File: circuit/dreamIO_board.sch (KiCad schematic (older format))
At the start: 49 parts

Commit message: finished circuit schematic. Needs review
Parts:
- added C? (x12): .1uF, symbol C
- added P?: CONN_01X03, symbol CONN_01X03
- added R? (x12): 150, symbol R
- added U? (x11): WS2812, symbol WS2812
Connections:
- net labels added: DOUT
- wire segments 154 -> 294
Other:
- note added: "MPU Connections"
- note added: "NeoPixel Output"
- moved on the sheet: C?, R?, U?

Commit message: added notes and updated circuit design
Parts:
- removed C? (x11): .1uF, symbol C
- removed R? (x11): 150, symbol R
- removed U? (x11): WS2812, symbol WS2812
- added C10, C11, C12, C15, C16, C17, C18, C19, C20, C21, C22: .1uF, symbol C
- added R13, R14, R15, R17, R18, R19, R20, R21, R22, R23, R24: 150, symbol R
- added U10, U11, U12, U13, U14, U15, U16, U6, U7, U8, U9: WS2812, symbol WS2812
- gave numbers to parts that had none: 52
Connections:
- wire segments 294 -> 258
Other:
- moved on the sheet: C9, R12

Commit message: added custom footprint for tsp61200 regulator
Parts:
- removed R13, R14, R15, R17, R18, R19, R20, R21, R22, R23, R24: 150, symbol R
- removed SW1: SPST, symbol SPST
- removed U10, U11, U12, U13, U14, U15, U16, U5, U6, U7, U8, U9: WS2812, symbol WS2812
- added LED1, LED10, LED11, LED12, LED2, LED3, LED4, LED5, LED6, LED7, LED8, LED9: WS2812B, kicad-libraries:WS2812B_LED, symbol WS2812B
- added SW1: SPDT, Buttons_Switches_ThroughHole:SW_Micro_SPST, symbol SPDT
- C1, C10, C11, C12, C13, C14, C15, C16, C17, C18, C19, C2, C20, C21, C22, C23, C24, C25, C26, C3, C4, C5, C6, C7, C8, C9, R1, R10, R11, R16, R2, R25, R26, R27, R3, R4, R5, R6, R7, R8, R9: footprint (none) -> kicad-libraries:0603
- D1: footprint (none) -> Capacitors_Tantalum_SMD:TantalC_SizeA_EIA-3216_HandSoldering
- IC1: footprint (none) -> Housings_DFN_QFN:DFN-10-1EP_3x3mm_Pitch0.5mm
- L1: footprint (none) -> kicad-libraries:1206E
- P1: value CONN_01X02 -> BATT; footprint (none) -> Pin_Headers:Pin_Header_Straight_1x02
- P2, P3, P5: footprint (none) -> Pin_Headers:Pin_Header_Straight_1x06
- P4, P6: footprint (none) -> Pin_Headers:Pin_Header_Straight_1x02
- P7: footprint (none) -> Pin_Headers:Pin_Header_Straight_1x03
- P8: footprint (none) -> Pin_Headers:Pin_Header_Straight_1x04
- P9: value CONN_01X03 -> PixelOut; footprint (none) -> Pin_Headers:Pin_Header_Straight_1x03
- R12: value 150 -> 220; footprint (none) -> kicad-libraries:0603
- SW2: value SW_PUSH -> RESET; footprint (none) -> shardy:SW_PUSH_SMALL
- SW3: value SW_PUSH -> PRGM; footprint (none) -> shardy:SW_PUSH_SMALL
- U1: footprint (none) -> kicad-libraries:SOT23-5
- U17: footprint (none) -> kicad-libraries:QFN-24-4x4-EP
- U2: footprint (none) -> open-project:MICRO-B_USB
- U3: footprint (none) -> kicad-libraries:SOT-223
- U4: footprint (none) -> ESP8266:ESP-12E
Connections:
- wire segments 258 -> 257
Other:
- moved on the sheet: C9, R12

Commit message: fixed IC1 footprint
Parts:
- IC1: footprint Housings_DFN_QFN:DFN-10-1EP_3x3mm_Pitch0.5mm -> tps61200_qfn_custom:tps61200_QFN-10_PAD
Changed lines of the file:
@@
 F 0 "IC1" H 4900 4400 50  0000 C CNN
 F 1 "TPS61200" H 5550 4400 50  0000 C CNN
-F 2 "Housings_DFN_QFN:DFN-10-1EP_3x3mm_Pitch0.5mm" H 5300 3800 60  0001 C CNN
+F 2 "tps61200_qfn_custom:tps61200_QFN-10_PAD" H 5300 3800 60  0001 C CNN
 F 3 "" H 5300 3800 60  0000 C CNN
 	1    5300 3800

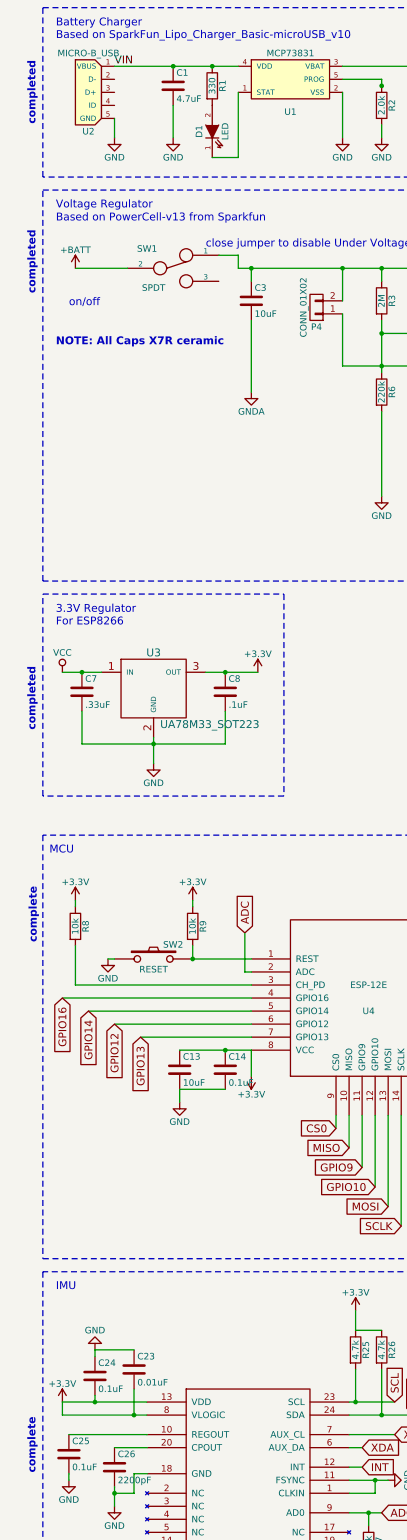
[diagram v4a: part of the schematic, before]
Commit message: grouped PCB components together for board:
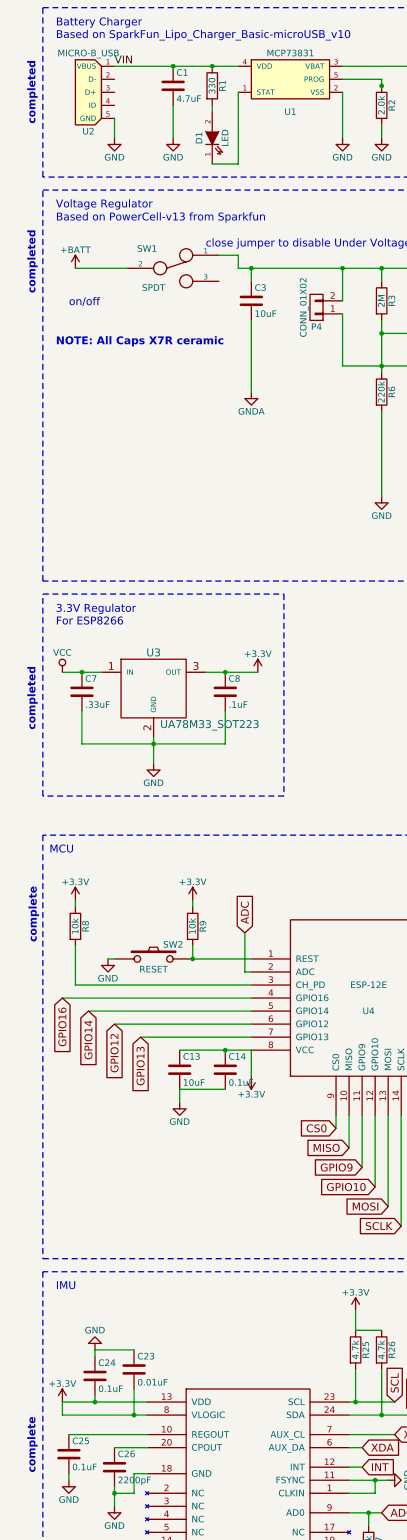
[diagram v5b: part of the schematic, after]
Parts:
- D1: footprint Capacitors_Tantalum_SMD:TantalC_SizeA_EIA-3216_HandSoldering -> kicad-libraries:0603
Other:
- moved on the sheet: D1
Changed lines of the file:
@@
 L LED D1
 U 1 1 56B0400A
-P 2500 1850
-F 0 "D1" H 2500 1950 50  0000 C CNN
-F 1 "LED" H 2500 1750 50  0000 C CNN
-F 2 "Capacitors_Tantalum_SMD:TantalC_SizeA_EIA-3216_HandSoldering" H 2500 1850 60  0001 C CNN
-F 3 "" H 2500 1850 60  0000 C CNN
-	1    2500 1850
+P 2500 1900
+F 0 "D1" H 2500 2000 50  0000 C CNN
+F 1 "LED" H 2500 1800 50  0000 C CNN
+F 2 "kicad-libraries:0603" H 2500 1900 60  0001 C CNN
+F 3 "" H 2500 1900 60  0000 C CNN
+	1    2500 1900
 	0    -1   -1   0
 $EndComp
@@
 	2000 12150 1900 12150
 Wire Wire Line
-	2000 11950 1750 11950
-Wire Wire Line
 	1750 12250 1750 12400
 Wire Wire Line
@@
 	2200 1650 2200 1900
 Wire Wire Line
-	2500 2050 2700 2050
-Wire Wire Line
-	2700 2050 2700 1550
+	2700 1550 2700 2100
 Wire Wire Line
 	1750 1350 2700 1350
@@
 Wire Wire Line
 	15200 11550 15700 11550
+Wire Wire Line
+	1750 11950 2000 11950
+Wire Wire Line
+	2500 1650 2500 1700
+Wire Wire Line
+	2700 2100 2500 2100
 $EndSCHEMATC

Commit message: finished layout
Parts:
- removed P2, P3: CONN_01X06, Pin_Headers:Pin_Header_Straight_1x06, symbol CONN_01X06
- removed P8: CONN_01X04, Pin_Headers:Pin_Header_Straight_1x04, symbol CONN_01X04
- added P2, P3: CONN_01X08, _connectors:_Pin2mm_8, symbol CONN_01X08
- P4: footprint Pin_Headers:Pin_Header_Straight_1x02 -> _connectors:_Solder_Pad2.54_2
- P5: footprint Pin_Headers:Pin_Header_Straight_1x06 -> _connectors:_Pin2mm_6
- P6: value CONN_01X02 -> gnd_con; footprint Pin_Headers:Pin_Header_Straight_1x02 -> _connectors:_Solder_Pad2.54_2
- P7: footprint Pin_Headers:Pin_Header_Straight_1x03 -> _connectors:_Solder_Pad2.54_3
- SW2, SW3: footprint shardy:SW_PUSH_SMALL -> kicad-libraries:SW_06_SMD
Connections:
- net +3V3: now also P2.8 (P8); no longer P5.6 (P6)
- net ADC: now also P2.2 (P2)
- net CS0: now also P5.1 (P1)
- net GND: now also P3.8 (P8); no longer P5.5 (P5)
- net GPIO0: now also P3.5 (P5)
- net GPIO10: now also P5.4 (P4)
- net GPIO12: now also P2.6 (P6)
- net GPIO13: now also P2.7 (P7)
- net GPIO14: now also P2.5 (P5)
- net GPIO15: now also P3.7 (P7)
- net GPIO16: now also P2.4 (P4)
- net GPIO2: now also P3.6 (P6)
- net GPIO4: now also P3.4 (P4)
- net GPIO5: now also P3.3 (P3)
- net GPIO9: now also P5.3 (P3)
- net MISO: now also P5.2 (P2)
- net MOSI: now also P5.5 (P5)
- net RX: now also P3.2 (P2); no longer P5.3 (P3)
- net SCLK: now also P5.6 (P6)
- net TX: now also P3.1 (P1); no longer P5.2 (P2)
- net VCC: no longer P5.4 (P4)
- net RESET: now reaches R9.2, SW2.2, U4.1 (REST)
- net RESET: now also P2.1 (P1)
- net CH_PD: now reaches R8.2, U4.3 (CH_PD)
- net CH_PD: now also P2.3 (P3)
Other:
- note removed: "FTDI"
- note removed: "SPI"
- moved on the sheet: P9

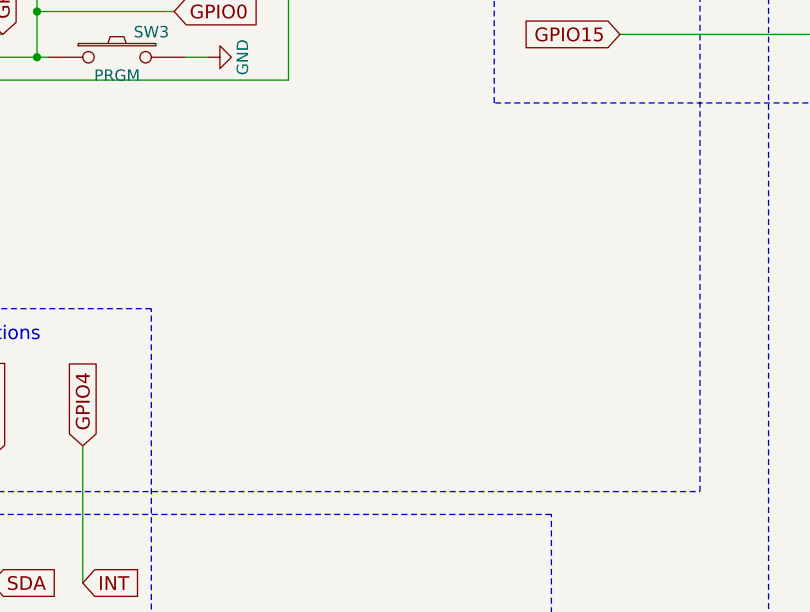
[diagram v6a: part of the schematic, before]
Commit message: added human input buttons
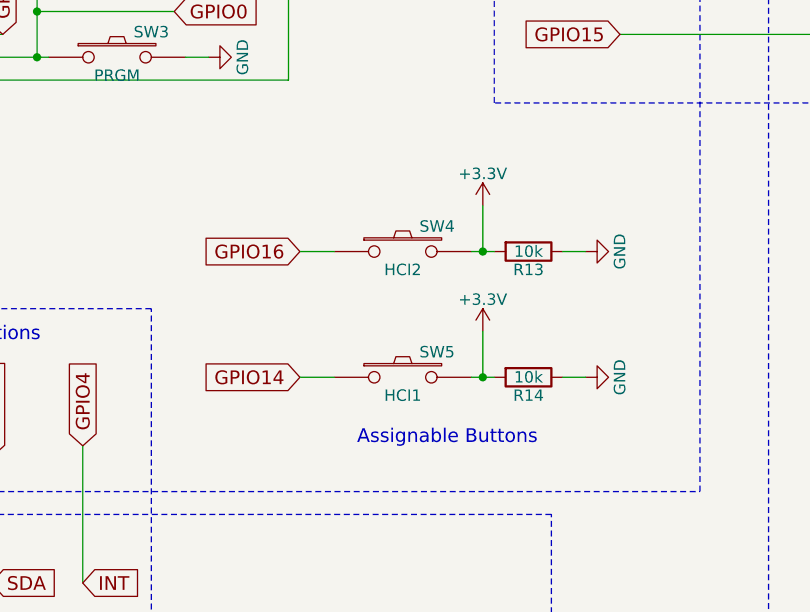
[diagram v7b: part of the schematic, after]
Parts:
- added R13, R14: 10k, kicad-libraries:0603, symbol R
- added SW4: HCI2, kicad-libraries:SW_06_SMD, symbol SW_PUSH
- added SW5: HCI1, kicad-libraries:SW_06_SMD, symbol SW_PUSH
- SW1: footprint Buttons_Switches_ThroughHole:SW_Micro_SPST -> dpst:DPST_TE_SSJ12R04
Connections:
- net +3V3: now also R13.2, R14.2, SW4.2, SW5.2
- net GND: now also R13.1, R14.1
- net GPIO14: now also SW5.1
- net GPIO16: now also SW4.1
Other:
- note added: "Assignable Buttons"
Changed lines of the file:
@@
 F 0 "SW1" H 2000 3050 50  0000 C CNN
 F 1 "SPDT" H 2050 2750 50  0000 C CNN
-F 2 "Buttons_Switches_ThroughHole:SW_Micro_SPST" H 2200 2900 60  0001 C CNN
+F 2 "dpst:DPST_TE_SSJ12R04" H 2200 2900 60  0001 C CNN
 F 3 "" H 2200 2900 60  0000 C CNN
 	1    2200 2900
@@
 Wire Wire Line
 	9750 3800 9750 3800
+$Comp
+L SW_PUSH SW4
+U 1 1 57392AE9
+P 7000 9450
+F 0 "SW4" H 7150 9560 50  0000 C CNN
+F 1 "HCI2" H 7000 9370 50  0000 C CNN
+F 2 "kicad-libraries:SW_06_SMD" H 7000 9450 60  0001 C CNN
+F 3 "" H 7000 9450 60  0000 C CNN
+	1    7000 9450
+	1    0    0    -1
+$EndComp
+$Comp
+L GND #PWR047
+U 1 1 57392AEF
+P 7800 9450
+F 0 "#PWR047" H 7800 9200 50  0001 C CNN
+F 1 "GND" H 7800 9300 50  0000 C CNN
+F 2 "" H 7800 9450 60  0000 C CNN
+F 3 "" H 7800 9450 60  0000 C CNN
+	1    7800 9450
+	0    -1   -1   0
+$EndComp
+$Comp
+L R R13
+U 1 1 57392BE0
+P 7550 9450
+F 0 "R13" V 7630 9450 50  0000 C CNN
+F 1 "10k" V 7550 9450 50  0000 C CNN
+F 2 "kicad-libraries:0603" V 7480 9450 30  0001 C CNN
+F 3 "" H 7550 9450 30  0000 C CNN
+	1    7550 9450
+	0    1    1    0
+$EndComp
+Wire Wire Line
+	7800 9450 7700 9450
+Wire Wire Line
+	7400 9450 7300 9450
+$Comp
+L +3.3V #PWR048
+U 1 1 573934AA
+P 7350 9250
+F 0 "#PWR048" H 7350 9100 50  0001 C CNN
+F 1 "+3.3V" H 7350 9390 50  0000 C CNN
+F 2 "" H 7350 9250 60  0000 C CNN
+F 3 "" H 7350 9250 60  0000 C CNN
+	1    7350 9250
+	1    0    0    -1
+$EndComp
+Wire Wire Line
+	7350 9250 7350 9450
+Connection ~ 7350 9450
+$Comp
+L SW_PUSH SW5
+U 1 1 5739382C
+P 7000 10000
+F 0 "SW5" H 7150 10110 50  0000 C CNN
+F 1 "HCI1" H 7000 9920 50  0000 C CNN
+F 2 "kicad-libraries:SW_06_SMD" H 7000 10000 60  0001 C CNN
+F 3 "" H 7000 10000 60  0000 C CNN
+	1    7000 10000
+	1    0    0    -1
+$EndComp
+$Comp
+L GND #PWR049
+U 1 1 57393832
+P 7800 10000
+F 0 "#PWR049" H 7800 9750 50  0001 C CNN
+F 1 "GND" H 7800 9850 50  0000 C CNN
+F 2 "" H 7800 10000 60  0000 C CNN
+F 3 "" H 7800 10000 60  0000 C CNN
+	1    7800 10000
+	0    -1   -1   0
+$EndComp
+$Comp
+L R R14
+U 1 1 57393838
+P 7550 10000
+F 0 "R14" V 7630 10000 50  0000 C CNN
+F 1 "10k" V 7550 10000 50  0000 C CNN
+F 2 "kicad-libraries:0603" V 7480 10000 30  0001 C CNN
+F 3 "" H 7550 10000 30  0000 C CNN
+	1    7550 10000
+	0    1    1    0
+$EndComp
+Wire Wire Line
+	7800 10000 7700 10000
+Wire Wire Line
+	7400 10000 7300 10000
+$Comp
+L +3.3V #PWR050
+U 1 1 57393840
+P 7350 9800
+F 0 "#PWR050" H 7350 9650 50  0001 C CNN
+F 1 "+3.3V" H 7350 9940 50  0000 C CNN
+F 2 "" H 7350 9800 60  0000 C CNN
+F 3 "" H 7350 9800 60  0000 C CNN
+	1    7350 9800
+	1    0    0    -1
+$EndComp
+Wire Wire Line
+	7350 9800 7350 10000
+Connection ~ 7350 10000
+Text GLabel 6550 9450 0    60   Input ~ 0
+GPIO16
+Text GLabel 6550 10000 0    60   Input ~ 0
+GPIO14
+Wire Wire Line
+	6550 9450 6700 9450
+Wire Wire Line
+	6550 10000 6700 10000
+Text Notes 6800 10300 0    60   ~ 0
+Assignable Buttons
 $EndSCHEMATC

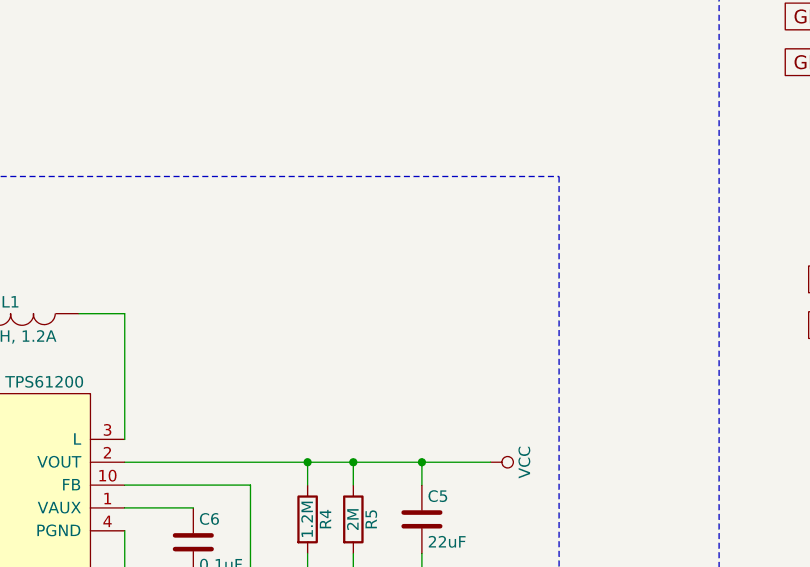
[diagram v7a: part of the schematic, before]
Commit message: realized the cascaded regulators might not be necessary since the output of the Neopixels at 3.3v is quite bright. While 5V would be brighter, it may not always be necessary to buy the extra parts
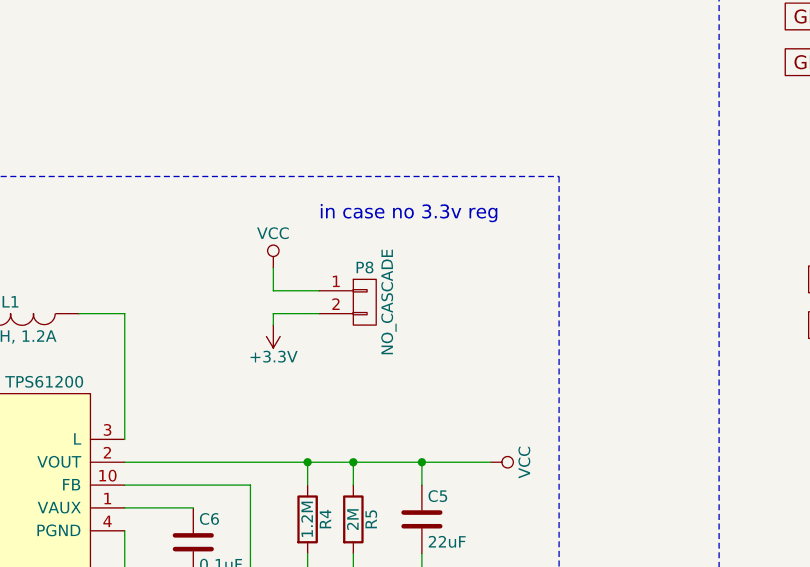
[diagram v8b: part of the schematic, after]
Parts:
- added P8: NO_CASCADE, _connectors:_Solder_Pad2.54_2, symbol CONN_01X02
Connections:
- net +3V3: now also P8.2 (P2)
- net VCC: now also P8.1 (P1)
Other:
- note added: "in case no 3.3v reg"
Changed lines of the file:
@@
 Text Notes 6800 10300 0    60   ~ 0
 Assignable Buttons
+$Comp
+L +3.3V #PWR051
+U 1 1 57396DBB
+P 6550 2950
+F 0 "#PWR051" H 6550 2800 50  0001 C CNN
+F 1 "+3.3V" H 6550 3090 50  0000 C CNN
+F 2 "" H 6550 2950 50  0000 C CNN
+F 3 "" H 6550 2950 50  0000 C CNN
+	1    6550 2950
+	-1   0    0    1
+$EndComp
+$Comp
+L CONN_01X02 P8
+U 1 1 57397254
+P 6950 2850
+F 0 "P8" H 6950 3000 50  0000 C CNN
+F 1 "NO_CASCADE" V 7050 2850 50  0000 C CNN
+F 2 "_connectors:_Solder_Pad2.54_2" H 6950 2850 60  0001 C CNN
+F 3 "" H 6950 2850 60  0000 C CNN
+	1    6950 2850
+	1    0    0    -1
+$EndComp
+$Comp
+L VCC #PWR052
+U 1 1 5739768F
+P 6550 2700
+F 0 "#PWR052" H 6550 2550 50  0001 C CNN
+F 1 "VCC" H 6550 2850 50  0000 C CNN
+F 2 "" H 6550 2700 50  0000 C CNN
+F 3 "" H 6550 2700 50  0000 C CNN
+	1    6550 2700
+	1    0    0    -1
+$EndComp
+Wire Wire Line
+	6750 2900 6550 2900
+Wire Wire Line
+	6550 2900 6550 2950
+Wire Wire Line
+	6750 2800 6550 2800
+Wire Wire Line
+	6550 2800 6550 2700
+Text Notes 6750 2500 0    60   ~ 0
+in case no 3.3v reg
 $EndSCHEMATC
